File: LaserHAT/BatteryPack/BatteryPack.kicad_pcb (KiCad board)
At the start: 2 copper layers, 100 x 100 mm, 140 parts, among them J1 TYPE-C-31-M-12, J3 B4B-PH-K-S(LF)(SN), J5 S5B-XH-A-1(LF)(SN), J6 S5B-XH-A-1(LF)(SN), J7 XT60PW-M, J8 XT60PW-M, Q1 AO3401A, Q10 AO3400A, Q11 AO3400A, Q12 AO3400A, Q13 AO3401A, Q14 AO3400A, Q15 AO3400A, Q16 AO3400A, Q17 AO3400A, Q18 AO3400A, Q6 AO3401A, Q7 AO3400A, Q8 AO3400A, Q9 AO3400A, SW1 CAX-MTS203M-YB-10.6JL, U1 LM393DR2G, U10 HY2213-BB3A, U11 HY2213-BB3A, U12 HY2213-BB3A, U13 HY2213-BB3A, U14 LM393DR2G, U15 LM393DR2G, U16 CJ431, U2 LM393DR2G, U3 CJ431, U4 CH224A, U5 CN3704, U6 HY2213-BB3A, U7 HY2213-BB3A, U8 HY2213-BB3A, U9 HY2213-BB3A

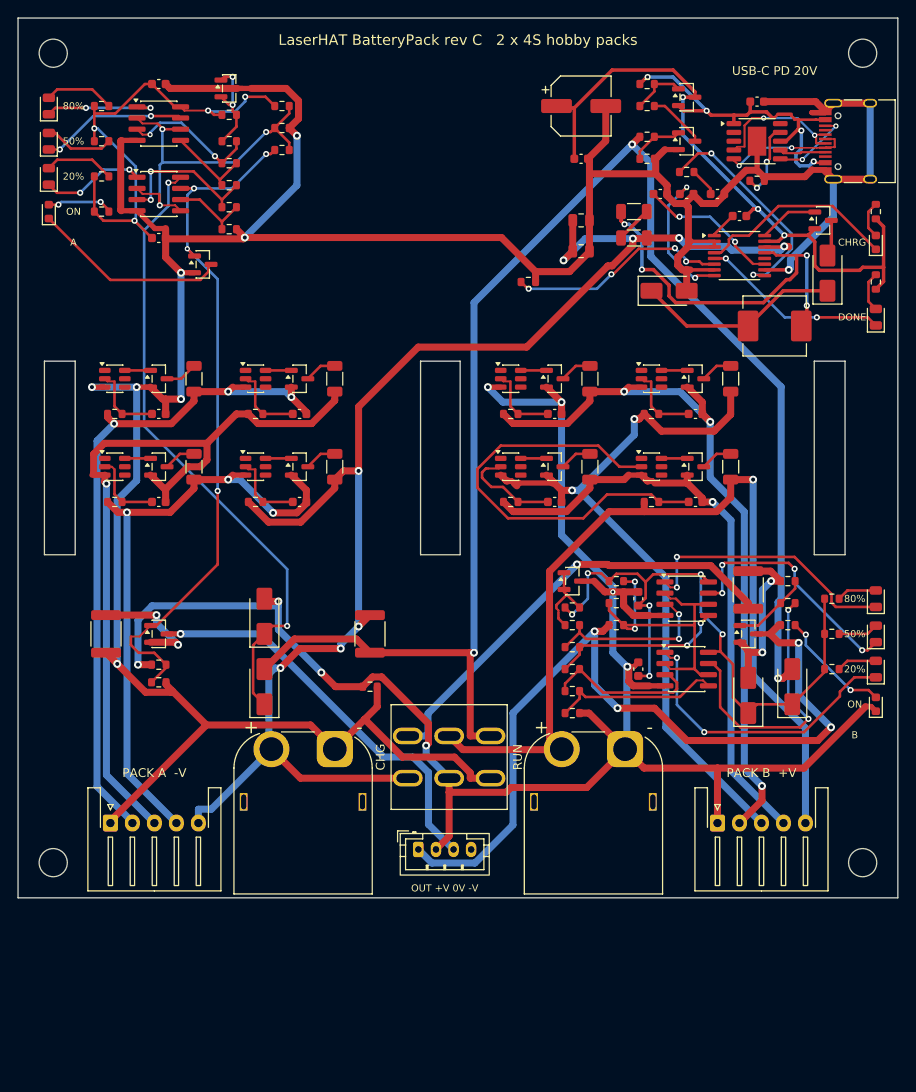
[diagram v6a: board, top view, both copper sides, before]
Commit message: BatteryPack: Raspberry Pi mounting holes (H5-H8, 58 x 49 M2.5) so the Pi + HAT sit above the board
Pi over y 4-60 on standoffs, ports end 11 mm past the right edge; toggle, pack sockets, output header and every
LED stay uncovered.  Balancer rows up 3 mm (pack B 1 mm left), CHRG / DONE LEDs to the top edge outside the Pi,
R9-R11 and C3 nudged, no-via rule areas under the standoffs.  Re-routed; one +SW pad entry hand-fixed for the
0.2 mm clearance.  DRC 0 / 0 / 0, ERC 0, path / sync 0, fab 136 placements / 44 BOM lines.

Co-Authored-By: Claude Fable 5.1 <noreply@anthropic.com>
Claude-Session: https://claude.ai/code/session_018vgLizGzYPynnY93ajvoVA
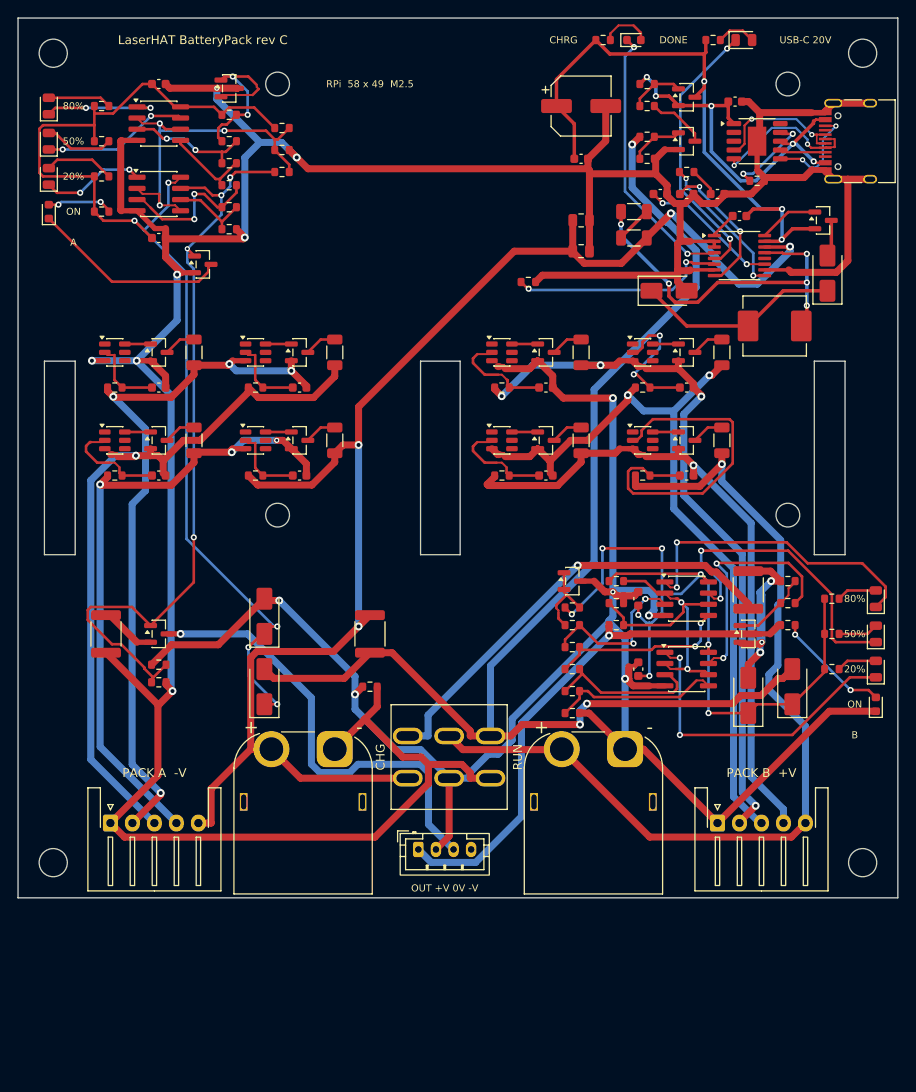
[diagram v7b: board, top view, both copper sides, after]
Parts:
- added H5: M2.5, MountingHole:MountingHole_2.7mm_M2.5, F.Cu at (29.5, 7.50)
- added H6: M2.5, MountingHole:MountingHole_2.7mm_M2.5, F.Cu at (87.5, 7.50)
- added H7: M2.5, MountingHole:MountingHole_2.7mm_M2.5, F.Cu at (29.5, 56.5)
- added H8: M2.5, MountingHole:MountingHole_2.7mm_M2.5, F.Cu at (87.5, 56.5)
- moved R28 36.6 mm to (66.5, 2.50), turned to 0 degrees
- moved D9 35.9 mm to (70.0, 2.50), turned to 0 degrees
- moved D10 34.9 mm to (82.5, 2.50), turned to 0 degrees
- moved R29 33.1 mm to (79.0, 2.50), turned to 0 degrees
- moved C16 3.16 mm to (60.0, 42.0)
- moved C17 3.16 mm to (76.0, 42.0)
- moved C18 3.16 mm to (60.0, 52.0)
- moved C19 3.16 mm to (76.0, 52.0)
- moved Q15 3.16 mm to (60.0, 38.0)
- moved Q16 3.16 mm to (76.0, 38.0)
- moved Q17 3.16 mm to (60.0, 48.0)
- moved Q18 3.16 mm to (76.0, 48.0)
- moved R58 3.16 mm to (55.0, 42.0)
- moved R59 3.16 mm to (71.0, 42.0)
- moved R60 3.16 mm to (55.0, 52.0)
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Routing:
- net +OUT: track 95.1 -> 60.4 mm, vias 4 -> 1
- net GND: track 371.9 -> 401.4 mm, vias 8 -> 7
- net +CHGB: track 174.0 -> 151.2 mm
- net +GB: track 74.2 -> 93.9 mm, vias 6 -> 8
- net Net-(U13-VDD): track 49.8 -> 39.4 mm
- net Net-(U5-COM2): track 26.1 -> 16.5 mm
- net /DONE: track 21.5 -> 30.9 mm
- net /VREF: track 11.4 -> 20.5 mm
- net /Q11_G: track 80.0 -> 89.0 mm
- net /CHRG: track 23.0 -> 31.1 mm, vias 0 -> 2
- net /C2: track 90.6 -> 83.2 mm
- net Net-(D13-K): track 27.7 -> 35.1 mm, vias 4 -> 2
- net Net-(U11-VDD): track 8.68 -> 15.7 mm, vias 0 -> 2
- net /GNDF: track 13.4 -> 6.34 mm, vias 2 -> 0
- net /B3: track 68.8 -> 74.9 mm
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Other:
- board text added: "LaserHAT BatteryPack rev C"
- board text added: "RPi 58 x 49 M2.5"
- board text added: "USB-C 20V"
- board text removed: "LaserHAT BatteryPack rev C 2 x 4S hobby packs"
- board text removed: "USB-C PD 20V"

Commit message: BatteryPack: LaserHAT outline on User.Comments, Raspberry Pi outline on User.Drawings
place.py copies the HAT's Edge.Cuts live from LaserDriver.kicad_pcb (MH1 onto H5, i.e. the
HAT sits at x 26-91, y 3.1-60 with its notch over the USB-C) and draws the Pi's 85 x 56
outline (x 26-111, y 4-60); both are drawings only, not in the gerbers.  Title silk moved
to (14, 30) so it is not under the HAT.  DRC 0/0/0, path/sync 0.

Co-Authored-By: Claude Fable 5.1 <noreply@anthropic.com>
Claude-Session: https://claude.ai/code/session_018vgLizGzYPynnY93ajvoVA
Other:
- board text added: "LaserHAT outline (MH1-MH4 on H5-H8)"
- board text added: "Raspberry Pi outline (85 x 56)"
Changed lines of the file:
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@@
 		(layer "B.SilkS")
 	)
+	(gr_arc
+		(start 26 7)
+		(mid 26.878679 4.878679)
+		(end 29 4)
+		(stroke
+			(width 0.15)
+			(type default)
+		)
+		(layer "Dwgs.User")
+	)
+	(gr_line
+		(start 26 57)
+		(end 26 7)
+		(stroke
+			(width 0.15)
+			(type default)
+		)
+		(layer "Dwgs.User")
+	)
+	(gr_line
+		(start 29 4)
+		(end 108 4)
+		(stroke
+			(width 0.15)
+			(type default)
+		)
+		(layer "Dwgs.User")
+	)
+	(gr_arc
+		(start 29 60)
+		(mid 26.878679 59.12132)
+		(end 26 57)
+		(stroke
+			(width 0.15)
+			(type default)
+		)
+		(layer "Dwgs.User")
+	)
+	(gr_arc
+		(start 108 4)
+		(mid 110.12132 4.878679)
+		(end 111 6.999999)
+		(stroke
+			(width 0.15)
+			(type default)
+		)
+		(layer "Dwgs.User")
+	)
+	(gr_line
+		(start 108 60)
+		(end 29 60)
+		(stroke
+			(width 0.15)
+			(type default)
+		)
+		(layer "Dwgs.User")
+	)
+	(gr_line
+		(start 111 7)
+		(end 111 57)
+		(stroke
+			(width 0.15)
+			(type default)
+		)
+		(layer "Dwgs.User")
+	)
+	(gr_arc
+		(start 111 57)
+		(mid 110.12132 59.12132)
+		(end 108 60)
+		(stroke
+			(width 0.15)
+			(type default)
+		)
+		(layer "Dwgs.User")
+	)
+	(gr_line
+		(start 26 6.121319)
+		(end 26 57)
+		(stroke
+			(width 0.15)
+			(type default)
+		)
+		(layer "Cmts.User")
+	)
+	(gr_arc
+		(start 26 6.12132)
+		(mid 26.87868 4)
+		(end 29 3.12132)
+		(stroke
+			(width 0.15)
+			(type default)
+		)
+		(layer "Cmts.User")
+	)
+	(gr_arc
+		(start 29 60)
+		(mid 26.87868 59.12132)
+		(end 26 57)
+		(stroke
+			(width 0.15)
+			(type default)
+		)
+		(layer "Cmts.User")
+	)
+	(gr_line
+		(start 29 60)
+		(end 88 60)
+		(stroke
+			(width 0.15)
+			(type default)
+		)
+		(layer "Cmts.User")
+	)
+	(gr_line
+		(start 85 11)
+		(end 91 11)
+		(stroke
+			(width 0.15)
+			(type default)
+		)
+		(layer "Cmts.User")
+	)
+	(gr_line
+		(start 85 19.5)
+		(end 85 11)
+		(stroke
+			(width 0.15)
+			(type default)
+		)
+		(layer "Cmts.User")
+	)
+	(gr_line
+		(start 88 3.121319)
+		(end 29 3.121319)
+		(stroke
+			(width 0.15)
+			(type default)
+		)
+		(layer "Cmts.User")
+	)
+	(gr_arc
+		(start 88 3.12132)
+		(mid 90.12132 4)
+		(end 91 6.12132)
+		(stroke
+			(width 0.15)
+			(type default)
+		)
+		(layer "Cmts.User")
+	)
+	(gr_line
+		(start 91 11)
+		(end 91 6.121319)
+		(stroke
+			(width 0.15)
+			(type default)
+		)
+		(layer "Cmts.User")
+	)
+	(gr_line
+		(start 91 19.5)
+		(end 85 19.5)
+		(stroke
+			(width 0.15)
+			(type default)
+		)
+		(layer "Cmts.User")
+	)
+	(gr_arc
+		(start 91 57)
+		(mid 90.12132 59.12132)
+		(end 88 60)
+		(stroke
+			(width 0.15)
+			(type default)
+		)
+		(layer "Cmts.User")
+	)
+	(gr_line
+		(start 91 57)
+		(end 91 19.5)
+		(stroke
+			(width 0.15)
+			(type default)
+		)
+		(layer "Cmts.User")
+	)
 	(gr_line
 		(start 0 0)
@@
 		)
 	)
-	(gr_text "PACK A  -V"
-		(at 15.5 85.8 0)
+	(gr_text "LaserHAT BatteryPack rev C"
+		(at 14 30 0)
 		(layer "F.SilkS")
 		(effects
@@
 		)
 	)
-	(gr_text "LaserHAT BatteryPack rev C"
-		(at 21 2.5 0)
+	(gr_text "PACK A  -V"
+		(at 15.5 85.8 0)
 		(layer "F.SilkS")
 		(effects
@@
 		)
 	)
+	(gr_text "Raspberry Pi outline (85 x 56)"
+		(at 68.5 62 0)
+		(layer "Dwgs.User")
+		(effects
+			(font
+				(size 1 1)
+				(thickness 0.15)
+			)
+		)
+	)
+	(gr_text "LaserHAT outline (MH1-MH4 on H5-H8)"
+		(at 58.5 58.05 0)
+		(layer "Cmts.User")
+		(effects
+			(font
+				(size 1 1)
+				(thickness 0.15)
+			)
+		)
+	)
 	(segment
 		(start 36 50.4854)
@@
 		(polygon
 			(pts
-				(xy 90 38.5) (xy 94.5 38.5) (xy 94.5 61.5) (xy 90 61.5)
+				(xy 45.25 38.5) (xy 50.75 38.5) (xy 50.75 61.5) (xy 45.25 61.5)
 			)
 		)
@@
 		(filled_areas_thickness no)
 		(keepout
-			(tracks not_allowed)
+			(tracks allowed)
 			(vias not_allowed)
 			(pads allowed)
@@
 		(polygon
 			(pts
-				(xy 2.5 38.5) (xy 7 38.5) (xy 7 61.5) (xy 2.5 61.5)
+				(xy 90.5 7.5) (xy 90.397777 8.276457) (xy 90.098076 9) (xy 89.62132 9.62132) (xy 89 10.098076) (xy 88.276457 10.397777)
+				(xy 87.5 10.5) (xy 86.723542 10.397777) (xy 86 10.098076) (xy 85.378679 9.62132) (xy 84.901923 9)
+				(xy 84.602222 8.276457) (xy 84.5 7.5) (xy 84.602222 6.723542) (xy 84.901923 6) (xy 85.378679 5.378679)
+				(xy 86 4.901923) (xy 86.723542 4.602222) (xy 87.5 4.5) (xy 88.276457 4.602222) (xy 89 4.901923)
+				(xy 89.62132 5.378679) (xy 90.098076 5.999999) (xy 90.397777 6.723542)
 			)
 		)
@@
 		(polygon
 			(pts
-				(xy 45.25 38.5) (xy 50.75 38.5) (xy 50.75 61.5) (xy 45.25 61.5)
+				(xy 2.5 38.5) (xy 7 38.5) (xy 7 61.5) (xy 2.5 61.5)
 			)
 		)
@@
 		(filled_areas_thickness no)
 		(keepout
-			(tracks allowed)
+			(tracks not_allowed)
 			(vias not_allowed)
 			(pads allowed)
@@
 		(polygon
 			(pts
-				(xy 90.5 56.5) (xy 90.397777 57.276457) (xy 90.098076 58) (xy 89.62132 58.62132) (xy 89 59.098076)
-				(xy 88.276457 59.397777) (xy 87.5 59.5) (xy 86.723542 59.397777) (xy 86 59.098076) (xy 85.378679 58.62132)
-				(xy 84.901923 58) (xy 84.602222 57.276457) (xy 84.5 56.5) (xy 84.602222 55.723542) (xy 84.901923 55)
-				(xy 85.378679 54.378679) (xy 86 53.901923) (xy 86.723542 53.602222) (xy 87.5 53.5) (xy 88.276457 53.602222)
-				(xy 89 53.901923) (xy 89.62132 54.378679) (xy 90.098076 55) (xy 90.397777 55.723542)
+				(xy 90 38.5) (xy 94.5 38.5) (xy 94.5 61.5) (xy 90 61.5)
 			)
 		)
@@
 		(polygon
 			(pts
-				(xy 90.5 7.5) (xy 90.397777 8.276457) (xy 90.098076 9) (xy 89.62132 9.62132) (xy 89 10.098076) (xy 88.276457 10.397777)
-				(xy 87.5 10.5) (xy 86.723542 10.397777) (xy 86 10.098076) (xy 85.378679 9.62132) (xy 84.901923 9)
-				(xy 84.602222 8.276457) (xy 84.5 7.5) (xy 84.602222 6.723542) (xy 84.901923 6) (xy 85.378679 5.378679)
-				(xy 86 4.901923) (xy 86.723542 4.602222) (xy 87.5 4.5) (xy 88.276457 4.602222) (xy 89 4.901923)
-				(xy 89.62132 5.378679) (xy 90.098076 5.999999) (xy 90.397777 6.723542)
+				(xy 32.5 56.5) (xy 32.397777 57.276457) (xy 32.098076 58) (xy 31.62132 58.62132) (xy 31 59.098076)
+				(xy 30.276457 59.397777) (xy 29.5 59.5) (xy 28.723542 59.397777) (xy 28 59.098076) (xy 27.378679 58.62132)
+				(xy 26.901923 58) (xy 26.602222 57.276457) (xy 26.5 56.5) (xy 26.602222 55.723542) (xy 26.901923 55)
+				(xy 27.378679 54.378679) (xy 28 53.901923) (xy 28.723542 53.602222) (xy 29.5 53.5) (xy 30.276457 53.602222)
+				(xy 31 53.901923) (xy 31.62132 54.378679) (xy 32.098076 55) (xy 32.397777 55.723542)
 			)
 		)
@@
 		(polygon
 			(pts
-				(xy 32.5 56.5) (xy 32.397777 57.276457) (xy 32.098076 58) (xy 31.62132 58.62132) (xy 31 59.098076)
-				(xy 30.276457 59.397777) (xy 29.5 59.5) (xy 28.723542 59.397777) (xy 28 59.098076) (xy 27.378679 58.62132)
-				(xy 26.901923 58) (xy 26.602222 57.276457) (xy 26.5 56.5) (xy 26.602222 55.723542) (xy 26.901923 55)
-				(xy 27.378679 54.378679) (xy 28 53.901923) (xy 28.723542 53.602222) (xy 29.5 53.5) (xy 30.276457 53.602222)
-				(xy 31 53.901923) (xy 31.62132 54.378679) (xy 32.098076 55) (xy 32.397777 55.723542)
+				(xy 90.5 56.5) (xy 90.397777 57.276457) (xy 90.098076 58) (xy 89.62132 58.62132) (xy 89 59.098076)
+				(xy 88.276457 59.397777) (xy 87.5 59.5) (xy 86.723542 59.397777) (xy 86 59.098076) (xy 85.378679 58.62132)
+				(xy 84.901923 58) (xy 84.602222 57.276457) (xy 84.5 56.5) (xy 84.602222 55.723542) (xy 84.901923 55)
+				(xy 85.378679 54.378679) (xy 86 53.901923) (xy 86.723542 53.602222) (xy 87.5 53.5) (xy 88.276457 53.602222)
+				(xy 89 53.901923) (xy 89.62132 54.378679) (xy 90.098076 55) (xy 90.397777 55.723542)
 			)
 		)
